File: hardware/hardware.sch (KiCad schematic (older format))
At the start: 25 parts, among them J1 Conn_01x04_Male, J2 DIN-5_180degree, J3 DIN-5_180degree, SW1 SW_Push, SW2 SW_Push, U1 Teensy3.2, U2 TeensyAudioShield3.2, U3 6N138

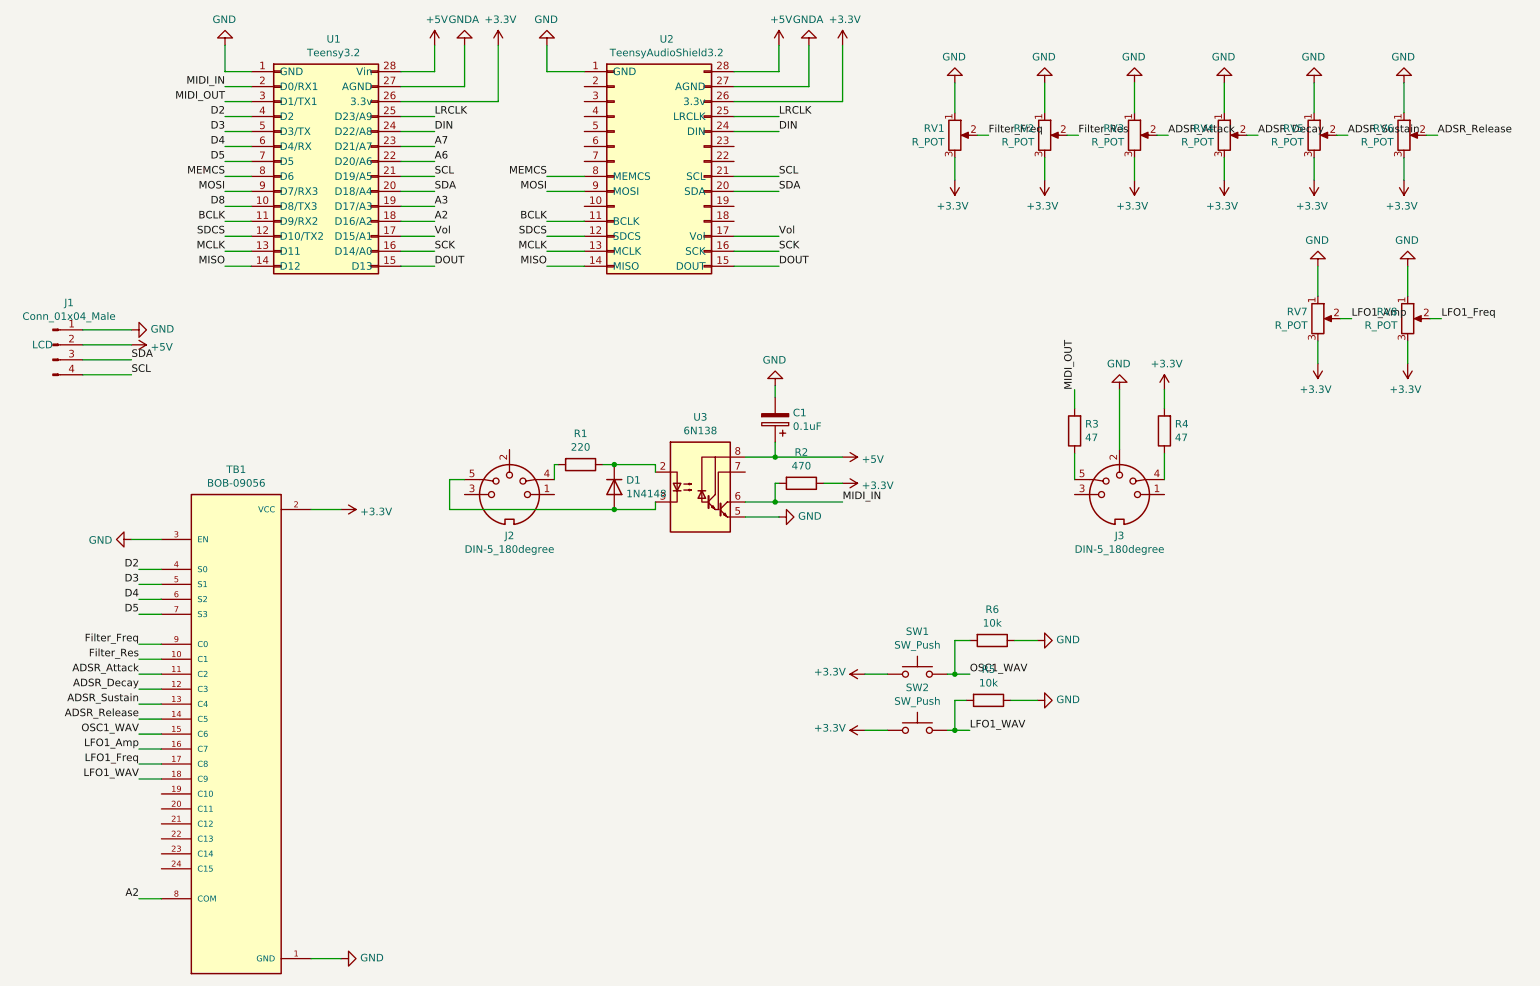
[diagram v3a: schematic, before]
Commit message: Remove MIDI out and add RGB LED header
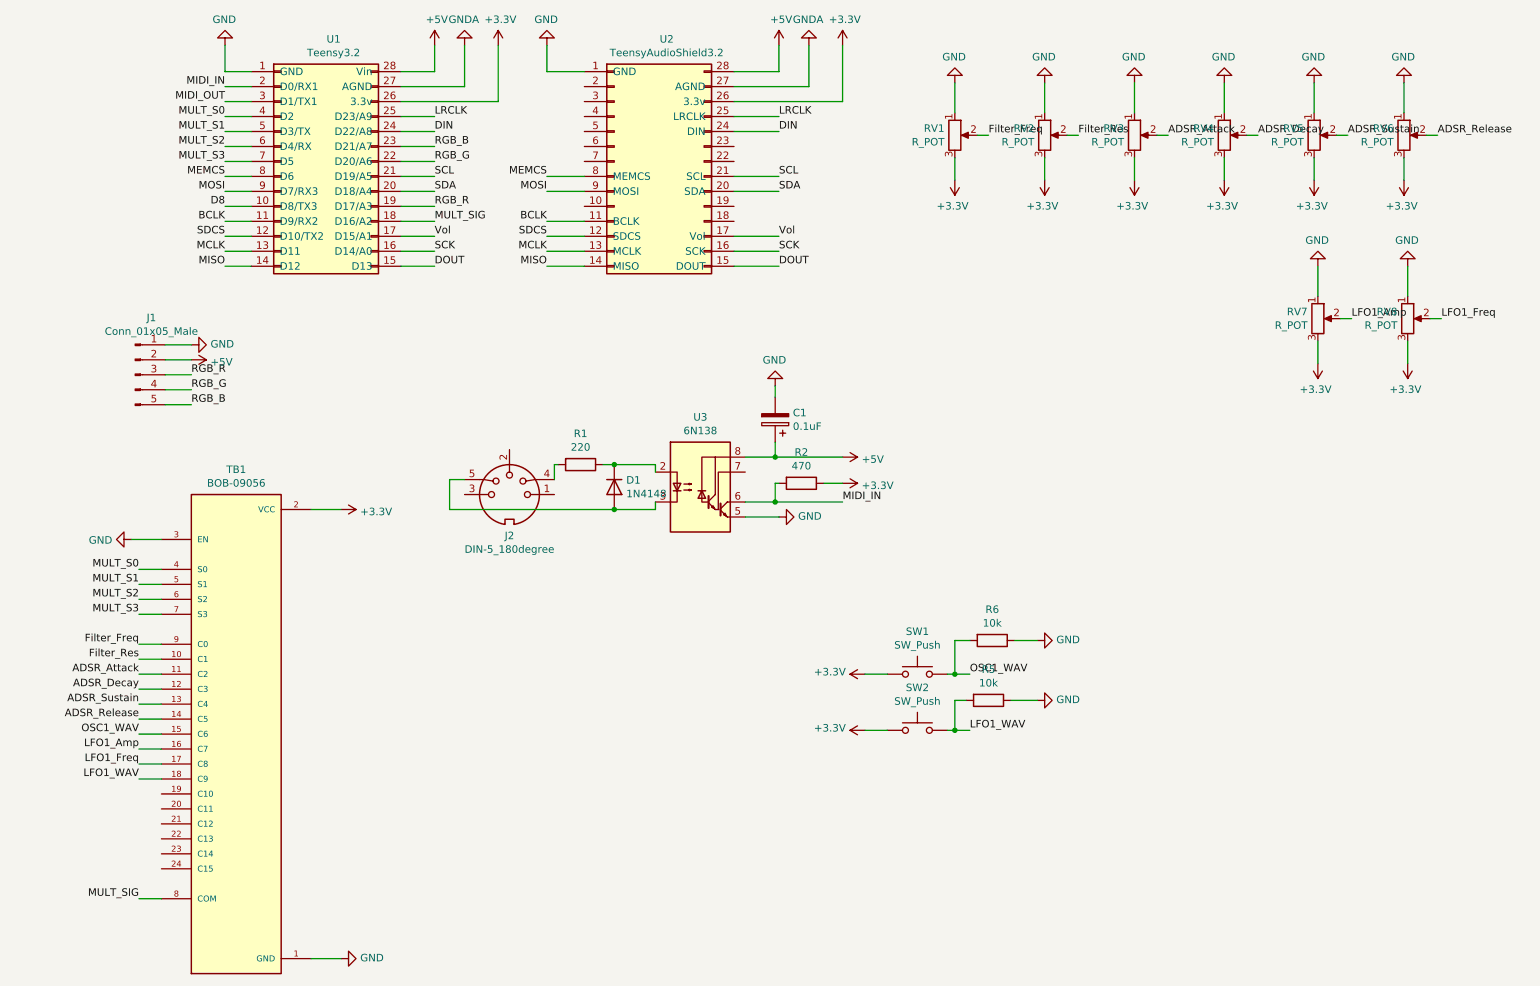
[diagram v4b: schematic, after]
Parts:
- removed J1: Conn_01x04_Male, Connector_PinHeader_2.54mm:PinHeader_1x04_P2.54mm_Vertical, symbol Connector:Conn_01x04_Male
- removed J3: DIN-5_180degree, Connector_PinHeader_2.54mm:PinHeader_1x05_P2.54mm_Vertical, symbol Connector:DIN-5_180degree
- removed R3, R4: 47, Resistor_THT:R_Axial_DIN0207_L6.3mm_D2.5mm_P10.16mm_Horizontal, symbol Device:R
- added J1: Conn_01x05_Male, Connector_PinHeader_2.54mm:PinHeader_1x05_P2.54mm_Vertical, symbol Connector:Conn_01x05_Male
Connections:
- net +5V: now also J1.2 (Pin_2)
- net GND: now also J1.1 (Pin_1)
- net A2 renamed MULT_SIG
- net A3 renamed RGB_R
- net RGB_R: now also J1.3 (Pin_3)
- net A6 renamed RGB_G
- net RGB_G: now also J1.4 (Pin_4)
- net A7 renamed RGB_B
- net RGB_B: now also J1.5 (Pin_5)
- net D2 renamed MULT_S0
- net D3 renamed MULT_S1
- net D4 renamed MULT_S2
- net D5 renamed MULT_S3
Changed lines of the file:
@@
 $EndDescr
-$Comp
-L Connector:DIN-5_180degree J3
-U 1 1 5FB453D9
-P 8100 4250
-F 0 "J3" H 8100 3975 50  0000 C CNN
-F 1 "DIN-5_180degree" H 8100 3884 50  0000 C CNN
-F 2 "Connector_PinHeader_2.54mm:PinHeader_1x05_P2.54mm_Vertical" H 8100 4250 50  0001 C CNN
-F 3 "http://www.mouser.com/ds/2/18/40_c091_abd_e-75918.pdf" H 8100 4250 50  0001 C CNN
-	1    8100 4250
-	-1   0    0    -1
-$EndComp
 $Comp
 L Connector:DIN-5_180degree J2
@@
 	1    4025 4250
 	-1   0    0    -1
-$EndComp
-$Comp
-L Connector:Conn_01x04_Male J1
-U 1 1 5FB467C1
-P 975 3250
-F 0 "J1" H 1083 3531 50  0000 C CNN
-F 1 "Conn_01x04_Male" H 1083 3440 50  0000 C CNN
-F 2 "Connector_PinHeader_2.54mm:PinHeader_1x04_P2.54mm_Vertical" H 975 3250 50  0001 C CNN
-F 3 "~" H 975 3250 50  0001 C CNN
-F 4 "LCD" H 975 3250 50  0000 R CNN "Name"
-	1    975  3250
-	1    0    0    -1
 $EndComp
 $Comp
@@
 Wire Wire Line
 	5525 1725 5825 1725
-$Comp
-L power:GND #PWR0109
-U 1 1 5FB78D65
-P 1500 3150
-F 0 "#PWR0109" H 1500 2900 50  0001 C CNN
-F 1 "GND" V 1505 3022 50  0000 R CNN
-F 2 "" H 1500 3150 50  0001 C CNN
-F 3 "" H 1500 3150 50  0001 C CNN
-	1    1500 3150
-	0    -1   -1   0
-$EndComp
-$Comp
-L power:+5V #PWR0110
-U 1 1 5FB79112
-P 1500 3250
-F 0 "#PWR0110" H 1500 3100 50  0001 C CNN
-F 1 "+5V" V 1515 3378 50  0000 L CNN
-F 2 "" H 1500 3250 50  0001 C CNN
-F 3 "" H 1500 3250 50  0001 C CNN
-	1    1500 3250
-	0    1    1    0
-$EndComp
-Text Label 1500 3350 0    50   ~ 0
-SDA
-Text Label 1500 3450 0    50   ~ 0
-SCL
-Wire Wire Line
-	1175 3150 1500 3150
-Wire Wire Line
-	1500 3250 1175 3250
-Wire Wire Line
-	1175 3350 1500 3350
-Wire Wire Line
-	1500 3450 1175 3450
 Text Label 2125 1525 2    50   ~ 0
 MIDI_IN
@@
 Wire Wire Line
 	5800 3600 5800 3525
-$Comp
-L power:GND #PWR0115
-U 1 1 5FB9ADFE
-P 8100 3550
-F 0 "#PWR0115" H 8100 3300 50  0001 C CNN
-F 1 "GND" H 8105 3377 50  0000 C CNN
-F 2 "" H 8100 3550 50  0001 C CNN
-F 3 "" H 8100 3550 50  0001 C CNN
-	1    8100 3550
-	-1   0    0    1
-$EndComp
-Wire Wire Line
-	8100 3550 8100 3950
-$Comp
-L power:+3.3V #PWR0116
-U 1 1 5FB9E85A
-P 8400 3550
-F 0 "#PWR0116" H 8400 3400 50  0001 C CNN
-F 1 "+3.3V" H 8415 3723 50  0000 C CNN
-F 2 "" H 8400 3550 50  0001 C CNN
-F 3 "" H 8400 3550 50  0001 C CNN
-	1    8400 3550
-	1    0    0    -1
-$EndComp
-$Comp
-L Device:R R4
-U 1 1 5FB9EBAF
-P 8400 3825
-F 0 "R4" H 8330 3779 50  0000 R CNN
-F 1 "47" H 8330 3870 50  0000 R CNN
-F 2 "Resistor_THT:R_Axial_DIN0207_L6.3mm_D2.5mm_P10.16mm_Horizontal" V 8330 3825 50  0001 C CNN
-F 3 "~" H 8400 3825 50  0001 C CNN
-	1    8400 3825
-	-1   0    0    1
-$EndComp
-Wire Wire Line
-	8400 3550 8400 3675
-Wire Wire Line
-	8400 3975 8400 4150
-Text Label 7800 3550 1    50   ~ 0
-MIDI_OUT
-$Comp
-L Device:R R3
-U 1 1 5FBA2CF8
-P 7800 3825
-F 0 "R3" H 7730 3779 50  0000 R CNN
-F 1 "47" H 7730 3870 50  0000 R CNN
-F 2 "Resistor_THT:R_Axial_DIN0207_L6.3mm_D2.5mm_P10.16mm_Horizontal" V 7730 3825 50  0001 C CNN
-F 3 "~" H 7800 3825 50  0001 C CNN
-	1    7800 3825
-	-1   0    0    1
-$EndComp
-Wire Wire Line
-	7800 3550 7800 3675
-Wire Wire Line
-	7800 3975 7800 4150
 Text Label 3525 2425 0    50   ~ 0
-A2
+MULT_SIG
 Text Label 3525 2325 0    50   ~ 0
-A3
+RGB_R
 Text Label 3525 2025 0    50   ~ 0
-A6
+RGB_G
 Text Label 3525 1925 0    50   ~ 0
-A7
+RGB_B
 Wire Wire Line
 	3300 1925 3525 1925
@@
 	3300 2425 3525 2425
 Text Label 2125 1725 2    50   ~ 0
-D2
+MULT_S0
 Text Label 2125 1825 2    50   ~ 0
-D3
+MULT_S1
 Text Label 2125 1925 2    50   ~ 0
-D4
+MULT_S2
 Text Label 2125 2025 2    50   ~ 0
-D5
+MULT_S3
 Text Label 2125 2325 2    50   ~ 0
 D8
@@
 	10225 1850 10150 1850
 Text Label 1550 6950 2    50   ~ 0
-A2
+MULT_SIG
 Wire Wire Line
 	1550 6950 1700 6950
 Text Label 1550 4750 2    50   ~ 0
-D2
+MULT_S0
 Text Label 1550 4850 2    50   ~ 0
-D3
+MULT_S1
 Text Label 1550 4950 2    50   ~ 0
-D4
+MULT_S2
 Text Label 1550 5050 2    50   ~ 0
-D5
+MULT_S3
 Wire Wire Line
 	1550 4750 1700 4750
@@
 Wire Wire Line
 	7375 5625 7550 5625
+$Comp
+L Connector:Conn_01x05_Male J1
+U 1 1 5FC915AD
+P 1525 3450
+F 0 "J1" H 1633 3831 50  0000 C CNN
+F 1 "Conn_01x05_Male" H 1633 3740 50  0000 C CNN
+F 2 "Connector_PinHeader_2.54mm:PinHeader_1x05_P2.54mm_Vertical" H 1525 3450 50  0001 C CNN
+F 3 "~" H 1525 3450 50  0001 C CNN
+	1    1525 3450
+	1    0    0    -1
+$EndComp
+$Comp
+L power:GND #PWR0109
+U 1 1 5FC9263B
+P 1900 3250
+F 0 "#PWR0109" H 1900 3000 50  0001 C CNN
+F 1 "GND" V 1905 3122 50  0000 R CNN
+F 2 "" H 1900 3250 50  0001 C CNN
+F 3 "" H 1900 3250 50  0001 C CNN
+	1    1900 3250
+	0    -1   -1   0
+$EndComp
+$Comp
+L power:+5V #PWR0110
+U 1 1 5FC92D02
+P 1900 3350
+F 0 "#PWR0110" H 1900 3200 50  0001 C CNN
+F 1 "+5V" V 1915 3478 50  0000 L CNN
+F 2 "" H 1900 3350 50  0001 C CNN
+F 3 "" H 1900 3350 50  0001 C CNN
+	1    1900 3350
+	0    1    1    0
+$EndComp
+Text Label 1900 3450 0    50   ~ 0
+RGB_R
+Text Label 1900 3550 0    50   ~ 0
+RGB_G
+Text Label 1900 3650 0    50   ~ 0
+RGB_B
+Wire Wire Line
+	1725 3250 1900 3250
+Wire Wire Line
+	1900 3350 1725 3350
+Wire Wire Line
+	1725 3450 1900 3450
+Wire Wire Line
+	1900 3550 1725 3550
+Wire Wire Line
+	1725 3650 1900 3650
 $EndSCHEMATC

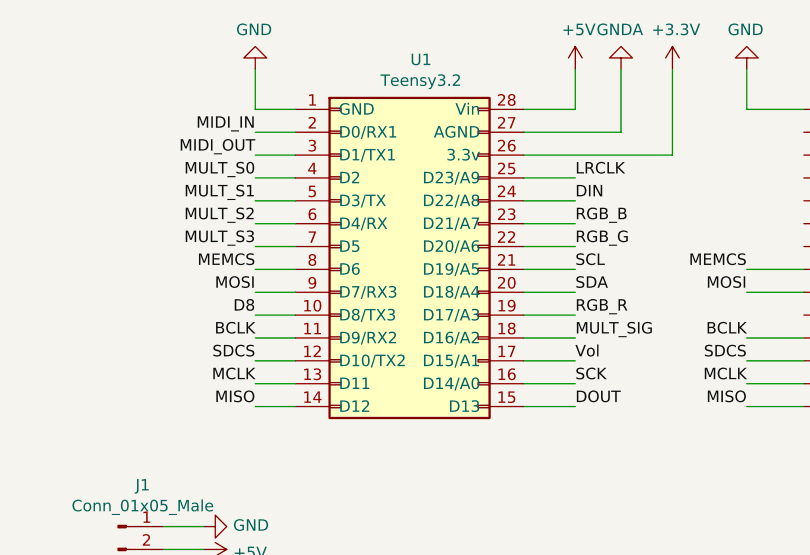
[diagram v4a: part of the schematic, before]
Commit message: Move RGB_R and MULT address pins to get RGB on PWM pin
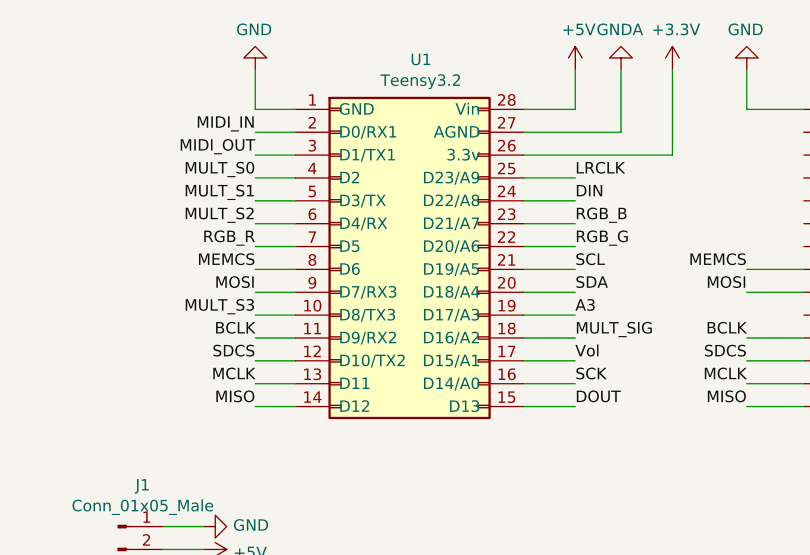
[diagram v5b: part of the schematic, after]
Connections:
- net D8 is gone; now on net MULT_S3: U1.10 (D8/TX3)
- net MULT_S3: no longer U1.7 (D5)
- net RGB_R: now also U1.7 (D5); no longer U1.19 (D17/A3)
- new net A3: U1.19 (D17/A3)
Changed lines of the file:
@@
 MULT_SIG
 Text Label 3525 2325 0    50   ~ 0
-RGB_R
+A3
 Text Label 3525 2025 0    50   ~ 0
 RGB_G
@@
 MULT_S2
 Text Label 2125 2025 2    50   ~ 0
+RGB_R
+Text Label 2125 2325 2    50   ~ 0
 MULT_S3
-Text Label 2125 2325 2    50   ~ 0
-D8
 Wire Wire Line
 	2125 1725 2300 1725
